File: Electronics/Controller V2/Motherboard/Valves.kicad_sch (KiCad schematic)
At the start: 7 parts, among them J1 Conn_01x08, J2 Conn_01x10

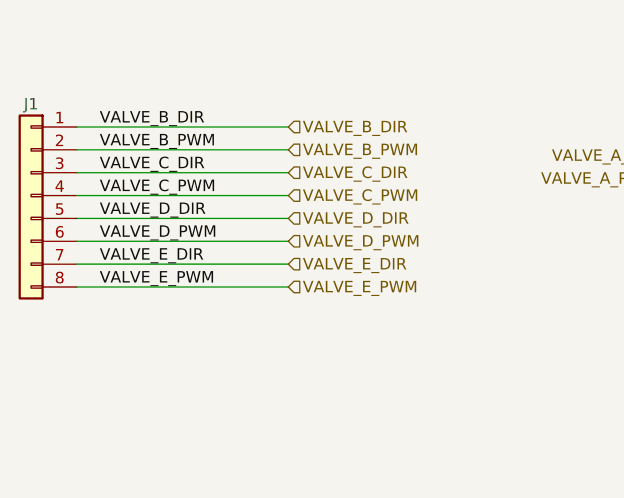
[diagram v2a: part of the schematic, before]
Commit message: Added relay to control output of valve E.
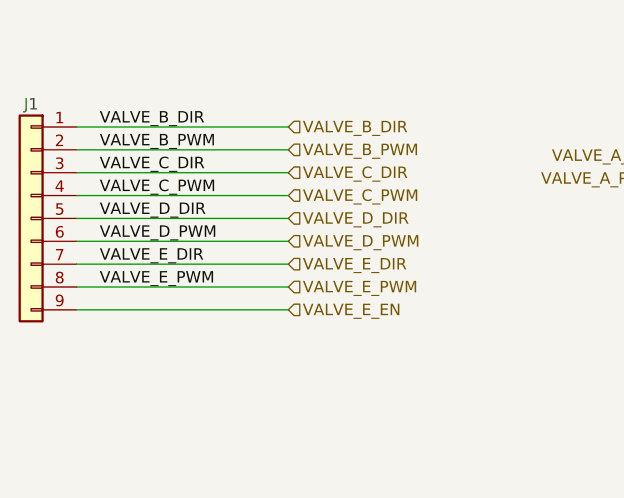
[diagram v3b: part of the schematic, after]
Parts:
- J1: footprint Connector_JST:JST_PH_B8B-PH-K_1x08_P2.00mm_Vertical -> Connector_JST:JST_PH_B9B-PH-K_1x09_P2.00mm_Vertical; symbol Connector_Generic:Conn_01x08 -> Connector_Generic:Conn_01x09
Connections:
- new net VALVE_E_EN: J1.9 (Pin_9)
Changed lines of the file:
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@@
   (title_block
     (title "Tandem Leveller Controller")
-    (date "2026-02-09")
+    (date "2026-03-01")
     (rev "V2.0")
     (company "(C) andy@britishideas.com 2026")
@@
     (stroke (width 0) (type default))
   )
+  (wire (pts (xy 55.245 95.25) (xy 78.74 95.25))
+    (stroke (width 0) (type default))
+  )
   (wire (pts (xy 121.285 78.105) (xy 130.81 78.105))
     (stroke (width 0) (type default))
@@
   )
   (hierarchical_label "VALVE_E_DIR" (shape input) (at 78.74 90.17 0) (fields_autoplaced)
+    (effects (font (size 1.27 1.27)) (justify left))
+  )
+  (hierarchical_label "VALVE_E_EN" (shape input) (at 78.74 95.25 0) (fields_autoplaced)
     (effects (font (size 1.27 1.27)) (justify left))
   )
@@
     )
   )
-  (symbol (lib_id "Connector_Generic:Conn_01x08") (at 50.165 82.55 0) (mirror y) (unit 1)
+  (symbol (lib_id "Connector_Generic:Conn_01x09") (at 50.165 85.09 0) (mirror y) (unit 1)
     (in_bom yes) (on_board yes) (dnp no)
     (property "Reference" "J1" (at 50.165 72.39 0)
       (effects (font (size 1.27 1.27)))
     )
-    (property "Value" "Conn_01x08" (at 50.165 73.66 0)
-      (effects (font (size 1.27 1.27)) hide)
-    )
-    (property "Footprint" "Connector_JST:JST_PH_B8B-PH-K_1x08_P2.00mm_Vertical" (at 50.165 82.55 0)
-      (effects (font (size 1.27 1.27)) hide)
-    )
-    (property "Datasheet" "~" (at 50.165 82.55 0)
+    (property "Value" "Conn_01x08" (at 50.165 76.2 0)
+      (effects (font (size 1.27 1.27)) hide)
+    )
+    (property "Footprint" "Connector_JST:JST_PH_B9B-PH-K_1x09_P2.00mm_Vertical" (at 50.165 85.09 0)
+      (effects (font (size 1.27 1.27)) hide)
+    )
+    (property "Datasheet" "~" (at 50.165 85.09 0)
       (effects (font (size 1.27 1.27)) hide)
     )
@@
     (pin "8")
     (pin "7")
-    (instances
-      (project "Tandem Leveller Controller V2"
+    (pin "9")
+    (instances
+      (project "Tandem Leveller Controller V2"

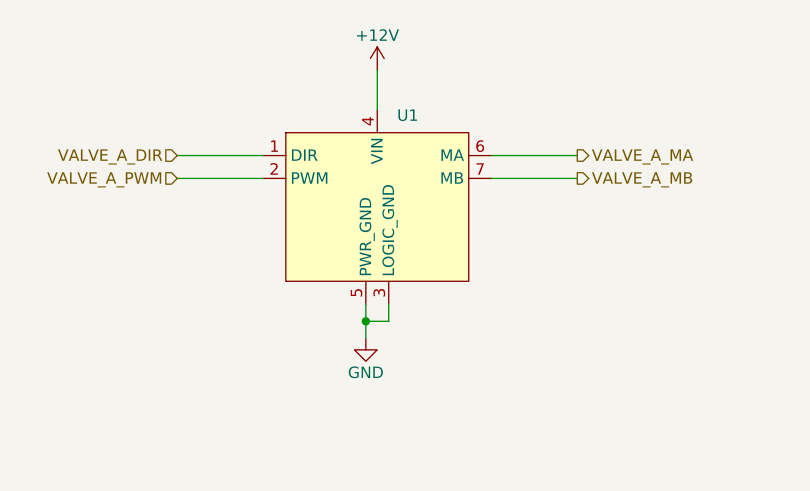
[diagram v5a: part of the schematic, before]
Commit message: Changed BMO085 from 5V to 3.3V to match Teensy.
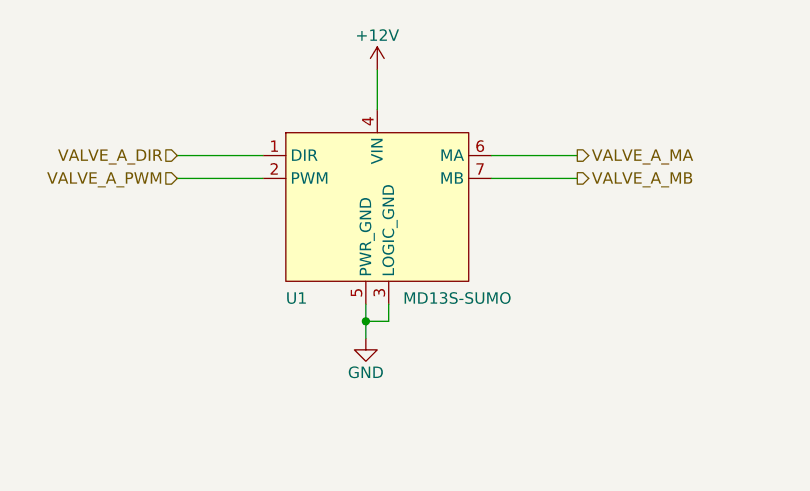
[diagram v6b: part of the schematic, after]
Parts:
- U1: value ~ -> MD13S-SUMO
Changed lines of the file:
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@@
   )
   (symbol (lib_id "BritishIdeas2:MD13S-SUMO") (at 133.35 92.075 0) (unit 1)
-    (in_bom yes) (on_board yes) (dnp no) (fields_autoplaced)
-    (property "Reference" "U1" (at 145.7041 73.66 0)
+    (in_bom yes) (on_board yes) (dnp no)
+    (property "Reference" "U1" (at 133.35 93.98 0)
       (effects (font (size 1.27 1.27)) (justify left))
     )
-    (property "Value" "~" (at 107.315 104.14 0)
+    (property "Value" "MD13S-SUMO" (at 152.4 93.98 0)
       (effects (font (size 1.27 1.27)))
     )
